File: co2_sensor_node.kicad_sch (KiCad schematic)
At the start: 27 parts, among them J1 Conn_01x03, J2 Conn_01x03, J3 Conn_01x02, J4 Conn_01x02, J5 Conn_01x03, J6 Conn_01x03

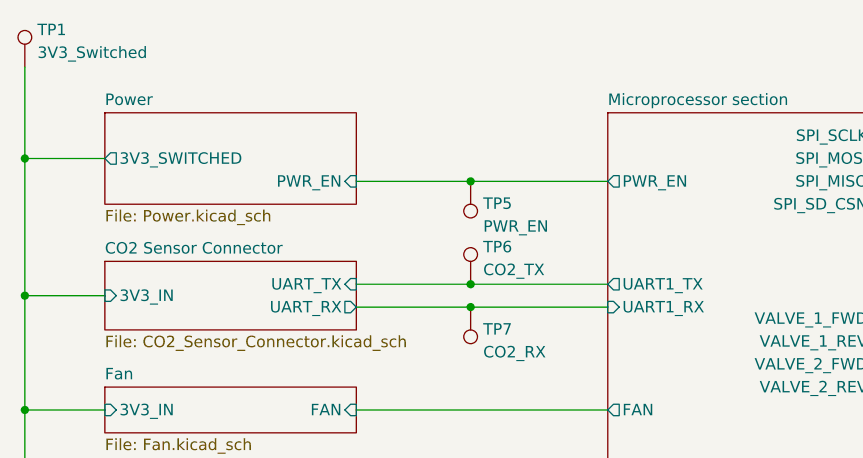
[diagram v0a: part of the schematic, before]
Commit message: Finish rev. 2 schematic and begin PCB layout
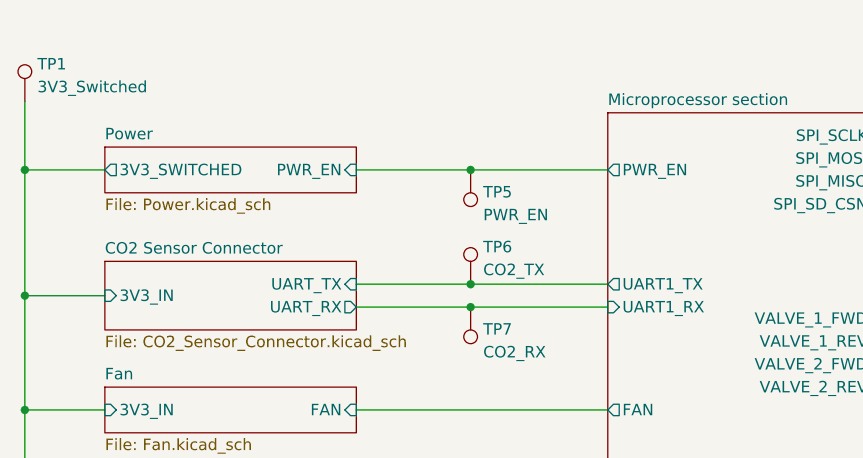
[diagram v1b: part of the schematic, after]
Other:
- moved on the sheet: TP1, TP5

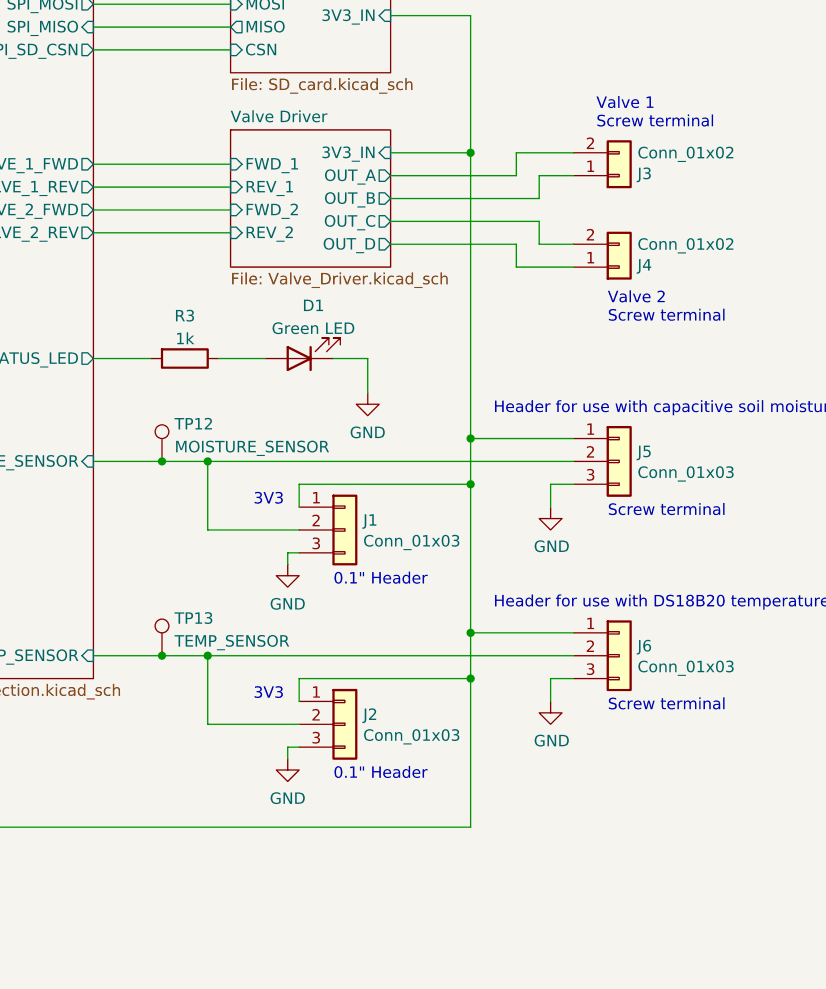
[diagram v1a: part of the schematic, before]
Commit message: Add 5V boost converter and begin redesign of PCB
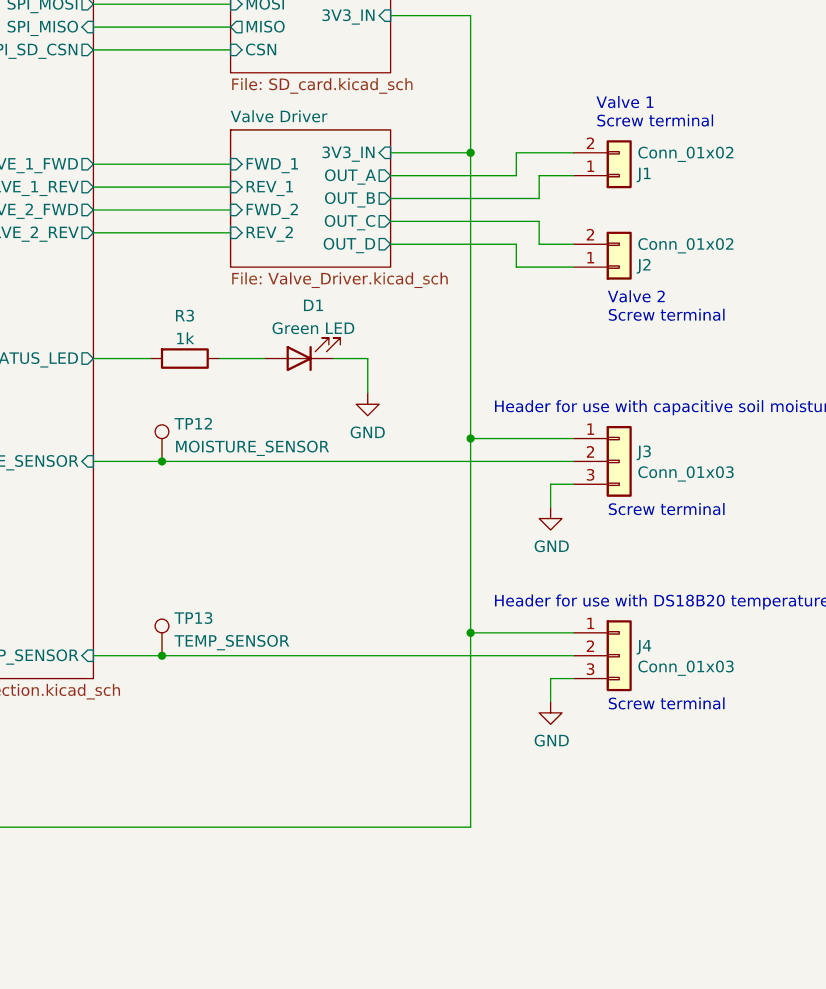
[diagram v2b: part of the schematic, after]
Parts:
- removed J1, J2: Conn_01x03, Connector_PinSocket_2.54mm:PinSocket_1x03_P2.54mm_Vertical, symbol Connector_Generic:Conn_01x03
- renumbered J3 to J1, J4 to J2, J5 to J3, J6 to J4
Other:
- note removed: "0.1" Header"
- note removed: "3V3"

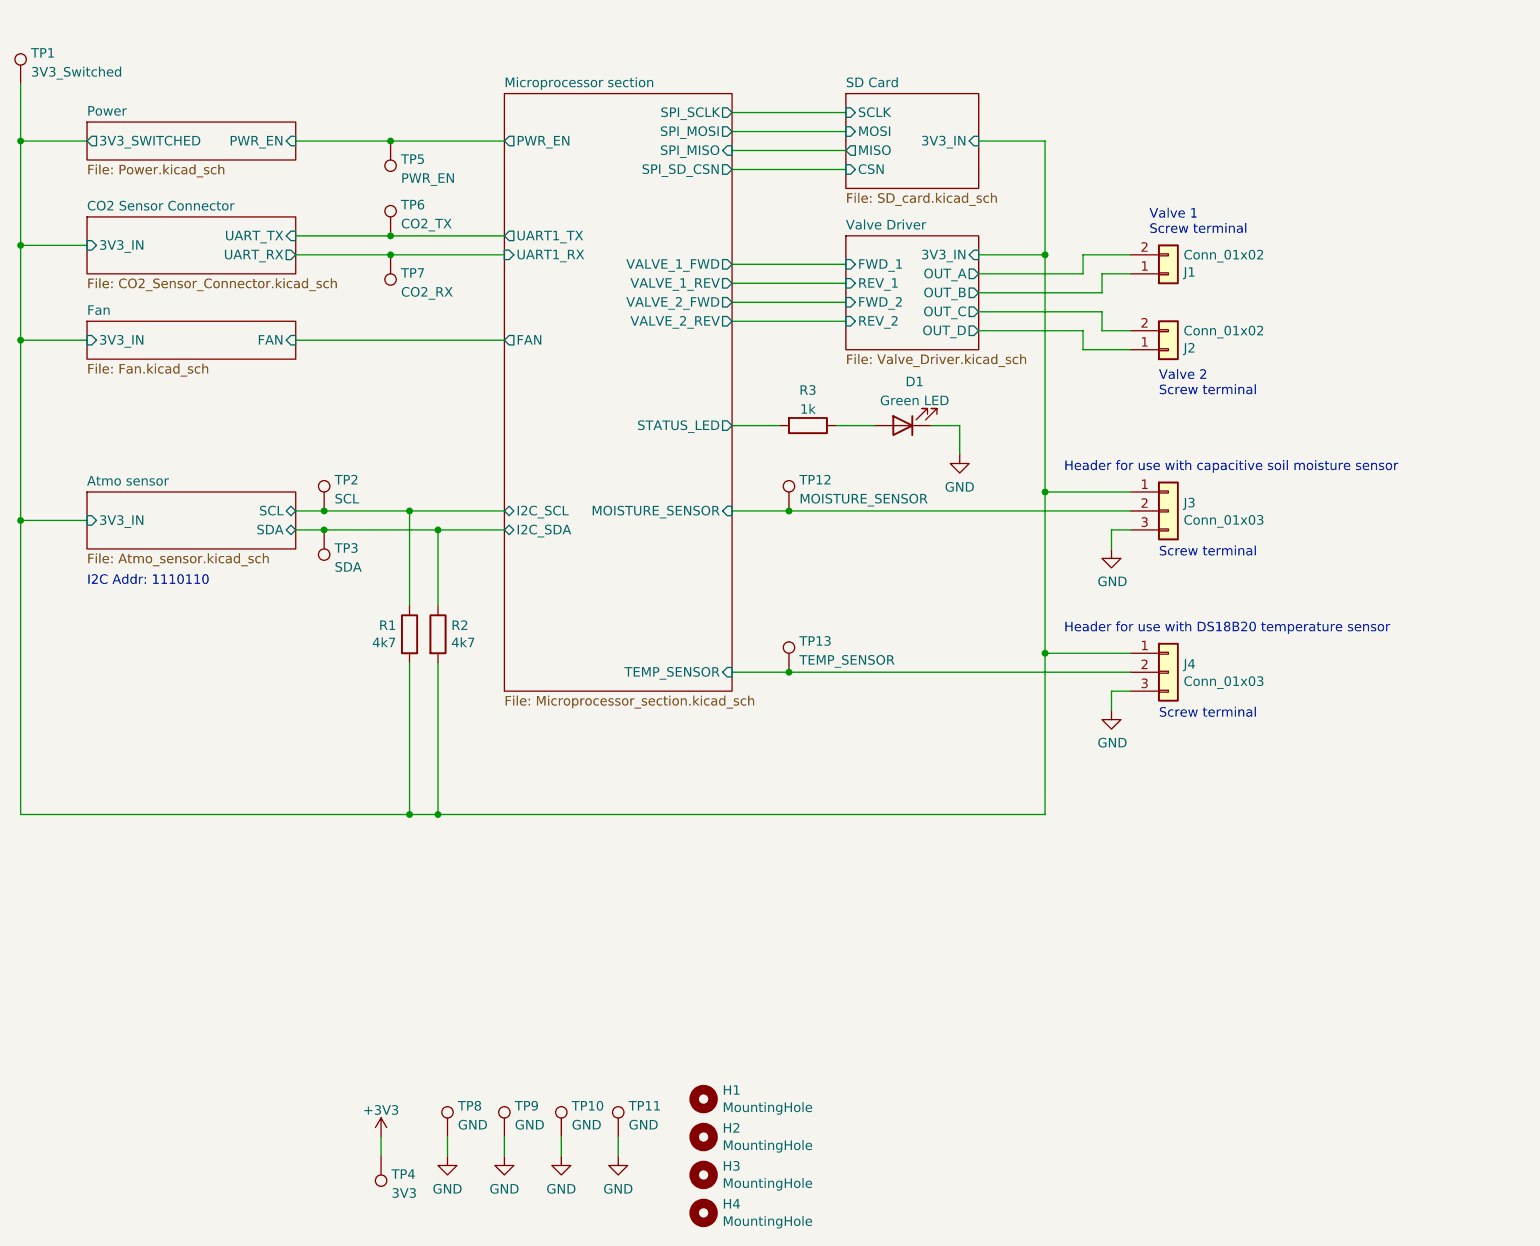
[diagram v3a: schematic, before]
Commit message: Finish component placement
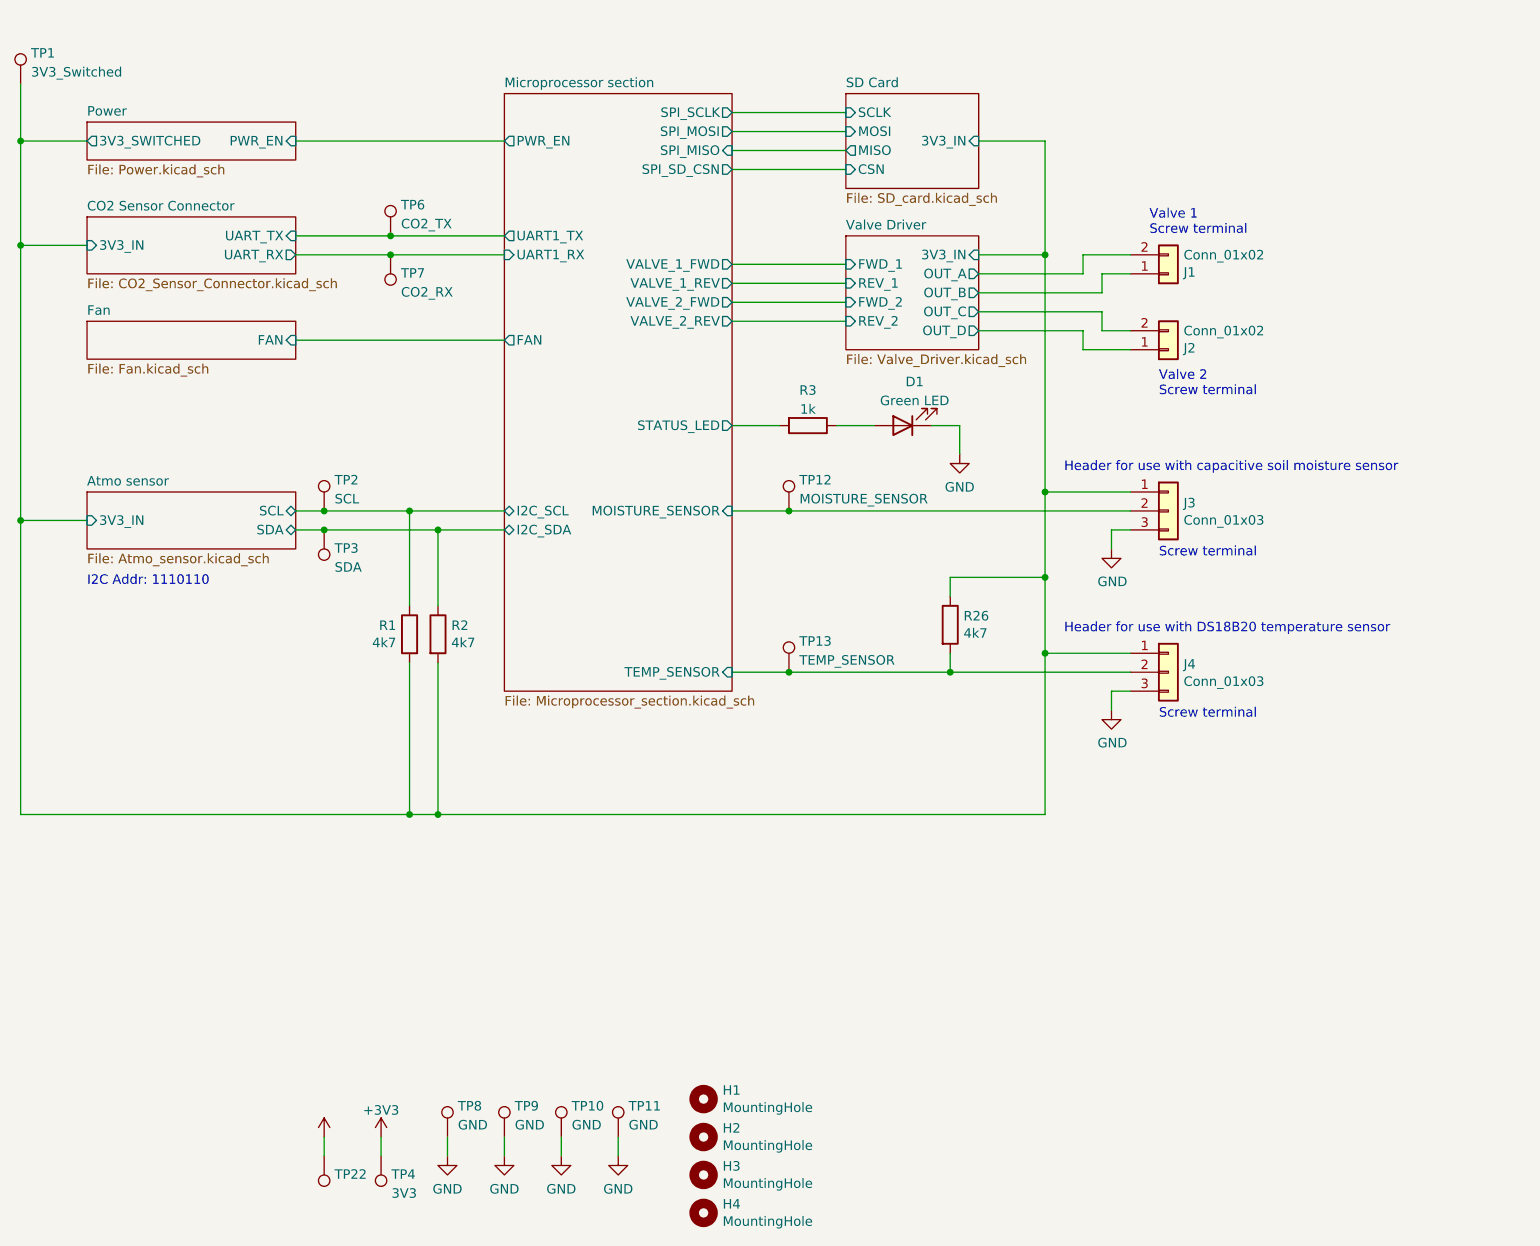
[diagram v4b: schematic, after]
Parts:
- removed TP5: PWR_EN, TestPoint:TestPoint_Loop_D2.50mm_Drill1.0mm_LowProfile, symbol Connector:TestPoint
- added R26: 4k7, Resistor_SMD:R_0603_1608Metric, symbol Device:R
- added TP22: (no value), symbol Connector:TestPoint
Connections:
- net Atmo sensor/3V3_IN: now also R26.1
- net Microprocessor section/TEMP_SENSOR: now also R26.2
- new net +5V: TP22.1
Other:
- sheet Fan ports: added none; removed 3V3_IN

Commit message: I was never here
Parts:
- renumbered R26 to R4, TP22 to TP4, TP4 to TP5

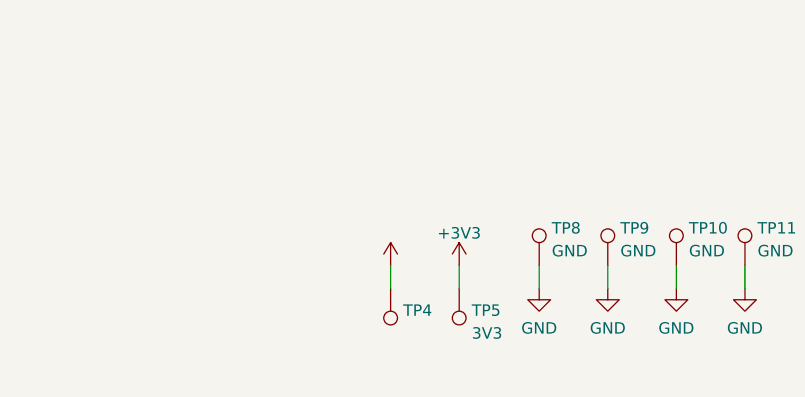
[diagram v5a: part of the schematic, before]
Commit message: Finish routing PCB revision 2
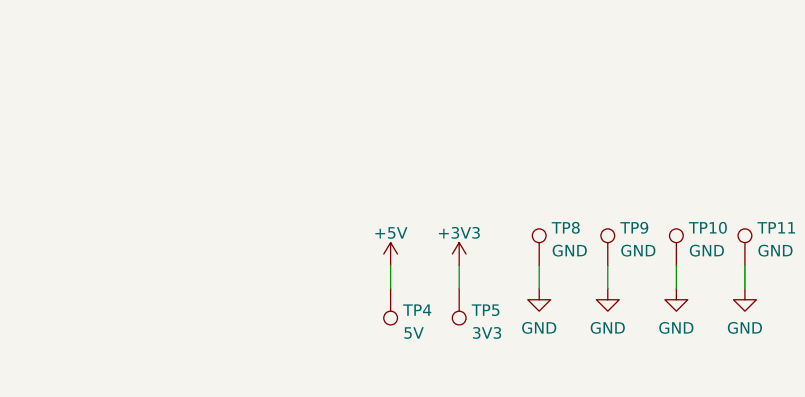
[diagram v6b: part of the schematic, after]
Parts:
- TP4: value (none) -> 5V; footprint (none) -> TestPoint:TestPoint_Loop_D2.50mm_Drill1.0mm_LowProfile
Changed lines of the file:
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@@
       (effects (font (size 1.27 1.27)) (justify right))
     )
-    (property "Value" "" (id 1) (at 106.807 185.3442 0)
-      (effects (font (size 1.27 1.27)) (justify right))
-    )
-    (property "Footprint" "" (id 2) (at 100.33 180.34 0)
+    (property "Value" "5V" (id 1) (at 106.807 185.3442 0)
+      (effects (font (size 1.27 1.27)) (justify right))
+    )
+    (property "Footprint" "TestPoint:TestPoint_Loop_D2.50mm_Drill1.0mm_LowProfile" (id 2) (at 100.33 180.34 0)
       (effects (font (size 1.27 1.27)) hide)
     )
@@
       (effects (font (size 1.27 1.27)) hide)
     )
-    (property "Value" "" (id 1) (at 105.41 174.2242 0))
+    (property "Value" "+5V" (id 1) (at 105.41 174.2242 0))
     (property "Footprint" "" (id 2) (at 105.41 177.8 0)
       (effects (font (size 1.27 1.27)) hide)
@@
       (reference "#PWR050") (unit 1) (value "GND") (footprint "")
     )
-    (path "/00000000-0000-0000-0000-000060a2751b/8d65a8c4-4cc5-40d9-b5bb-ef45a343ad02"
-      (reference "#PWR051") (unit 1) (value "+3V3") (footprint "")
-    )
     (path "/00000000-0000-0000-0000-000060a2751b/a834bc54-983b-4b4a-93c8-eb7b17abe4bf"
       (reference "#PWR052") (unit 1) (value "GND") (footprint "")
@@
       (reference "JP2") (unit 1) (value "BOOT_JP") (footprint "Connector_PinHeader_2.54mm:PinHeader_1x02_P2.54mm_Vertical")
     )
+    (path "/00000000-0000-0000-0000-000060a2751b/d37997e2-8d0e-4e99-81fa-141d822e78fb"
+      (reference "JP3") (unit 1) (value "USB_PWR_JP") (footprint "Connector_PinHeader_2.54mm:PinHeader_1x02_P2.54mm_Vertical")
+    )
     (path "/00000000-0000-0000-0000-000060ad9954/063a059b-b84b-4c0c-a31e-6675ab18fc7a"

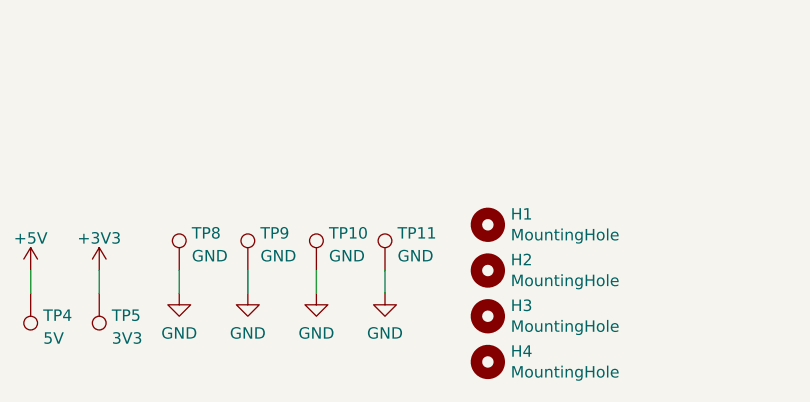
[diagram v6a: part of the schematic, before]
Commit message: Finish routing round 2
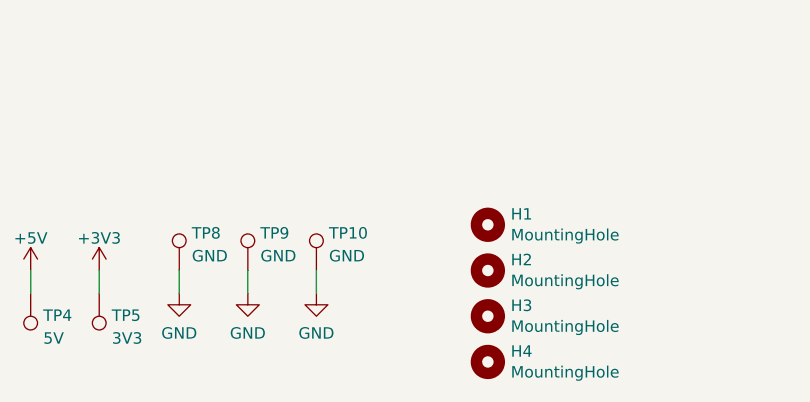
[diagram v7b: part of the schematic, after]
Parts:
- removed TP11: GND, TestPoint:TestPoint_Loop_D2.50mm_Drill1.0mm_LowProfile, symbol Connector:TestPoint
